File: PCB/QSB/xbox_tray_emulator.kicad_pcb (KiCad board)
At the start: 2 copper layers, 10.2 x 29.6 mm, 6 parts, among them J1 to Xbox, U1 ATtiny13A-S, U2 AP2127N-3.3

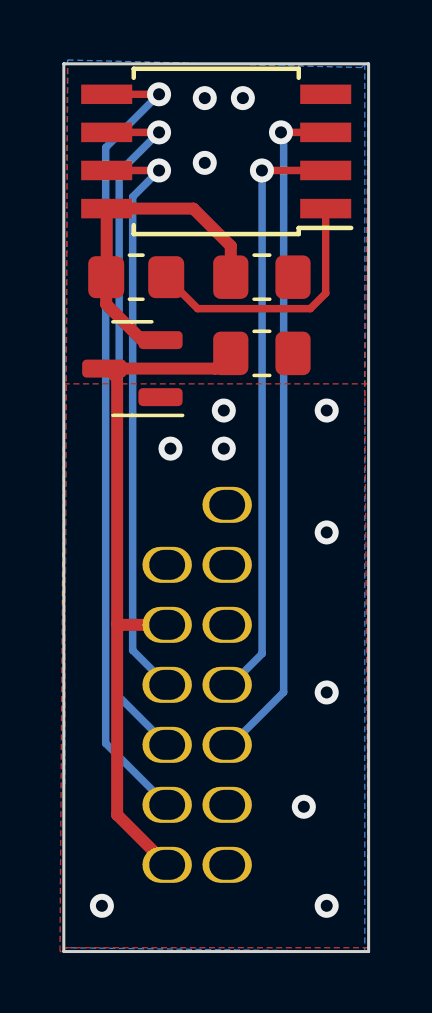
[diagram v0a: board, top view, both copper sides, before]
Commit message: shrink PCB a little
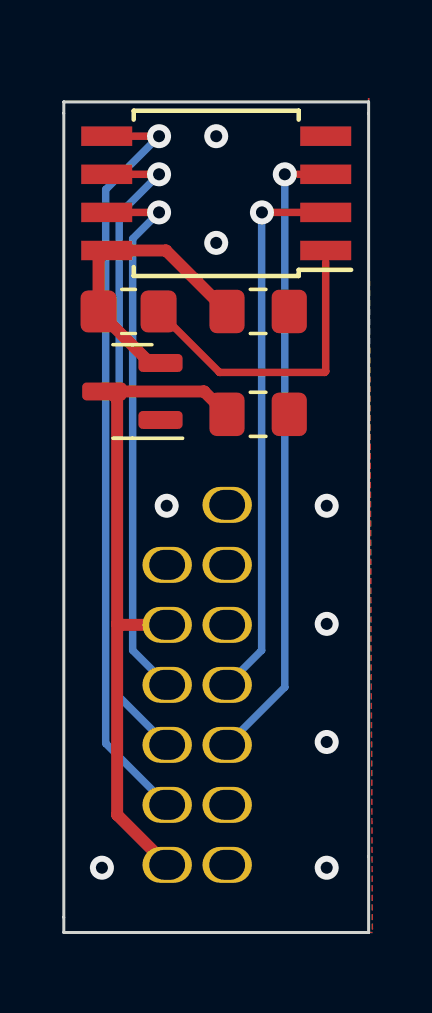
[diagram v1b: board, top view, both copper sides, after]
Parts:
- moved C2 2.04 mm to (143.6, 68.5)
- moved U1 1.40 mm to (142.2, 61.1)
- moved R1 1.17 mm to (139.3, 65.0)
- moved C1 1.15 mm to (143.6, 65.0)
- moved U2 0.76 mm to (139.4, 67.7)
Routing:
- net Net-(J1-Pad5): track 22.9 -> 20.8 mm
- net Net-(J1-Pad7): track 19.9 -> 18.0 mm
- net /Net-(R1-Pad1): track 11.4 -> 9.77 mm
- net Net-(J1-Pad4): track 27.0 -> 25.6 mm
- net Net-(J1-Pad6): track 23.4 -> 22.0 mm
- net Net-(J1-Pad8): track 19.7 -> 18.3 mm
- net Net-(R1-Pad2): track 8.79 -> 10.1 mm
- net /Net-(J1-Pad10): track 23.5 -> 22.7 mm
- net Net-(C1-Pad2): vias 12 -> 8
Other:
- board size 10.2 x 29.6 mm -> 10.2 x 27.7 mm

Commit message: increase U1 pads for "narrow" ATtiny13
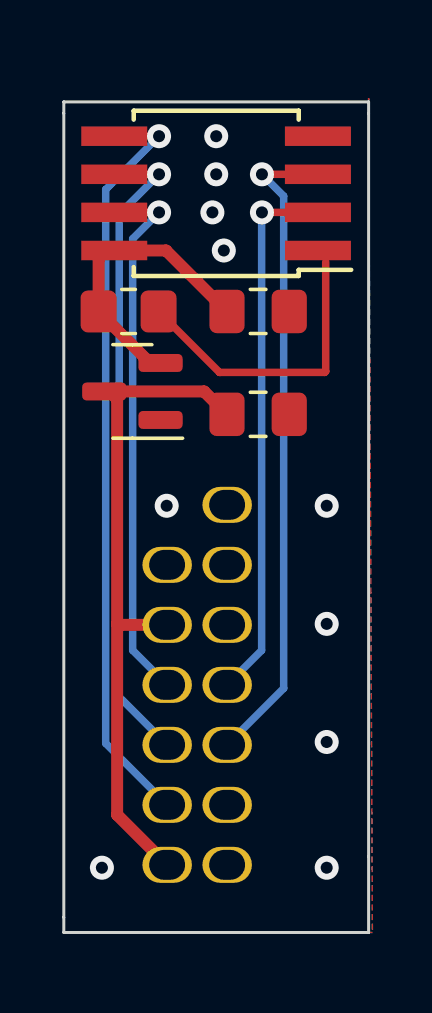
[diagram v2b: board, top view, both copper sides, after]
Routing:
- net Net-(J1-Pad5): track 20.8 -> 22.0 mm
- net Net-(C1-Pad2): vias 8 -> 10
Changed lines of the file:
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@@
     (fp_line (start -2.65 2.65) (end -2.65 -1.65) (layer "F.Fab") (width 0.15))
     (fp_line (start 2.65 2.65) (end -2.65 2.65) (layer "F.Fab") (width 0.15))
-    (pad "1" smd rect (at -3.65 -1.905 180) (size 1.7 0.65) (layers "F.Cu" "F.Paste" "F.Mask")
+    (pad "1" smd rect (at -3.39 -1.905 180) (size 2.2 0.65) (layers "F.Cu" "F.Paste" "F.Mask")
       (net 9 "Net-(R1-Pad2)") (pinfunction "~{RESET}/PB5") (pintype "bidirectional"))
-    (pad "2" smd rect (at -3.65 -0.635 180) (size 1.7 0.65) (layers "F.Cu" "F.Paste" "F.Mask")
+    (pad "2" smd rect (at -3.39 -0.635 180) (size 2.2 0.65) (layers "F.Cu" "F.Paste" "F.Mask")
       (net 6 "Net-(J1-Pad7)") (pinfunction "PB3") (pintype "bidirectional"))
-    (pad "3" smd rect (at -3.65 0.635 180) (size 1.7 0.65) (layers "F.Cu" "F.Paste" "F.Mask")
+    (pad "3" smd rect (at -3.39 0.635 180) (size 2.2 0.65) (layers "F.Cu" "F.Paste" "F.Mask")
       (net 4 "Net-(J1-Pad5)") (pinfunction "PB4") (pintype "bidirectional"))
-    (pad "4" smd rect (at -3.65 1.905 180) (size 1.7 0.65) (layers "F.Cu" "F.Paste" "F.Mask")
+    (pad "4" smd rect (at -3.39 1.905 180) (size 2.2 0.65) (layers "F.Cu" "F.Paste" "F.Mask")
       (net 12 "Net-(C1-Pad2)") (pinfunction "GND") (pintype "power_in"))
-    (pad "5" smd rect (at 3.65 1.905 180) (size 1.7 0.65) (layers "F.Cu" "F.Paste" "F.Mask")
+    (pad "5" smd rect (at 3.4 1.905 180) (size 2.2 0.65) (layers "F.Cu" "F.Paste" "F.Mask")
       (net 8 "Net-(J1-Pad4)") (pinfunction "PB0") (pintype "bidirectional"))
-    (pad "6" smd rect (at 3.65 0.635 180) (size 1.7 0.65) (layers "F.Cu" "F.Paste" "F.Mask")
+    (pad "6" smd rect (at 3.4 0.635 180) (size 2.2 0.65) (layers "F.Cu" "F.Paste" "F.Mask")
       (net 5 "Net-(J1-Pad6)") (pinfunction "PB1") (pintype "bidirectional"))
-    (pad "7" smd rect (at 3.65 -0.635 180) (size 1.7 0.65) (layers "F.Cu" "F.Paste" "F.Mask")
+    (pad "7" smd rect (at 3.4 -0.635 180) (size 2.2 0.65) (layers "F.Cu" "F.Paste" "F.Mask")
       (net 7 "Net-(J1-Pad8)") (pinfunction "PB2") (pintype "bidirectional"))
-    (pad "8" smd rect (at 3.65 -1.905 180) (size 1.7 0.65) (layers "F.Cu" "F.Paste" "F.Mask")
+    (pad "8" smd rect (at 3.4 -1.905 180) (size 2.2 0.65) (layers "F.Cu" "F.Paste" "F.Mask")
       (net 10 "/Net-(R1-Pad1)") (pinfunction "VCC") (pintype "power_in"))
     (model "${KICAD6_3DMODEL_DIR}/Package_SO.3dshapes/SOIC-8W_5.3x5.3mm_P1.27mm.wrl"
@@
   (gr_line (start 147.32 58.039) (end 137.16 58.039) (layer "Edge.Cuts") (width 0.1))
   (gr_line (start 147.32 58.42) (end 147.32 83.185) (layer "Edge.Cuts") (width 0.1))
-  (segment (start 145.89 60.452) (end 144.526 60.452) (width 0.25) (layer "F.Cu") (net 4))
-  (via (at 144.526 60.452) (size 0.8) (drill 0.4) (layers "F.Cu" "B.Cu") (net 4))
-  (segment (start 142.605 79.47) (end 144.526 77.549) (width 0.25) (layer "B.Cu") (net 4))
-  (segment (start 144.526 77.549) (end 144.526 60.833) (width 0.25) (layer "B.Cu") (net 4))
+  (segment (start 145.63 60.452) (end 143.764 60.452) (width 0.25) (layer "F.Cu") (net 4))
+  (via (at 143.764 60.452) (size 0.8) (drill 0.4) (layers "F.Cu" "B.Cu") (net 4))
+  (segment (start 144.489 61.177) (end 143.764 60.452) (width 0.25) (layer "B.Cu") (net 4))
+  (segment (start 144.489 77.586) (end 144.489 61.177) (width 0.25) (layer "B.Cu") (net 4))
+  (segment (start 142.605 79.47) (end 144.489 77.586) (width 0.25) (layer "B.Cu") (net 4))
   (segment (start 138.59 60.452) (end 140.335 60.452) (width 0.25) (layer "F.Cu") (net 5))
   (via (at 140.335 60.452) (size 0.8) (drill 0.4) (layers "F.Cu" "B.Cu") (net 5))
@@
   (via (at 145.923 71.501) (size 0.8) (drill 0.4) (layers "F.Cu" "B.Cu") (free) (net 12))
   (via (at 145.923 79.375) (size 0.8) (drill 0.4) (layers "F.Cu" "B.Cu") (free) (net 12))
+  (via (at 142.113 61.722) (size 0.8) (drill 0.4) (layers "F.Cu" "B.Cu") (free) (net 12))
+  (via (at 142.24 60.452) (size 0.8) (drill 0.4) (layers "F.Cu" "B.Cu") (free) (net 12))
   (via (at 142.24 59.182) (size 0.8) (drill 0.4) (layers "F.Cu" "B.Cu") (free) (net 12))
-  (via (at 142.24 62.738) (size 0.8) (drill 0.4) (layers "F.Cu" "B.Cu") (free) (net 12))
   (via (at 145.923 83.566) (size 0.8) (drill 0.4) (layers "F.Cu" "B.Cu") (free) (net 12))
   (via (at 140.589 71.501) (size 0.8) (drill 0.4) (layers "F.Cu" "B.Cu") (free) (net 12))
+  (via (at 142.494 62.992) (size 0.8) (drill 0.4) (layers "F.Cu" "B.Cu") (free) (net 12))
   (via (at 138.43 83.566) (size 0.8) (drill 0.4) (layers "F.Cu" "B.Cu") (free) (net 12))
   (via (at 145.923 75.438) (size 0.8) (drill 0.4) (layers "F.Cu" "B.Cu") (free) (net 12))
